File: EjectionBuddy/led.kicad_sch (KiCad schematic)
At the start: 10 parts

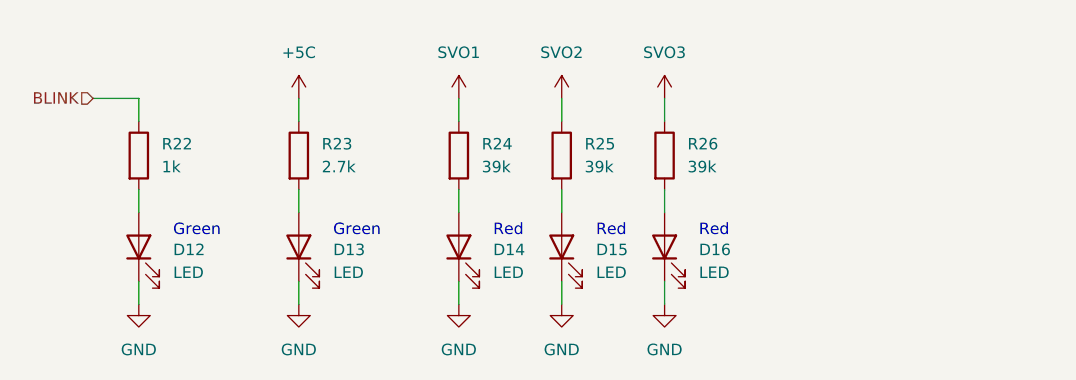
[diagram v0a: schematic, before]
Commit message: Side-mcu stm -> attiny, with improvements here and there
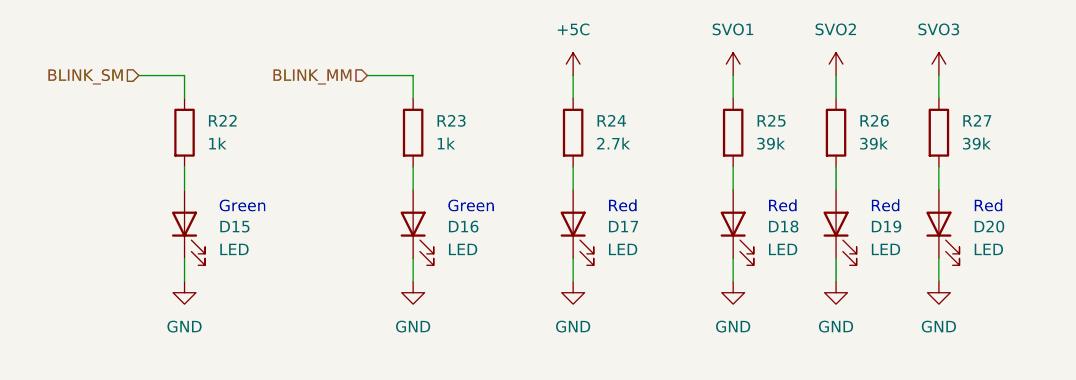
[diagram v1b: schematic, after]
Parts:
- added D15: LED, LED_SMD:LED_0603_1608Metric, symbol Device:LED
- added R22: 1k, Resistor_SMD:R_0603_1608Metric, symbol Device:R
- renumbered D12 to D16, D13 to D17, D14 to D18, D15 to D19, D16 to D20, R22 to R23, R23 to R24, R24 to R25, R25 to R26, R26 to R27
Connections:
- net GND: now also D15.1 (K)
- net BLINK renamed BLINK_MM
- new net: D15.2 (A), R22.2
- new net BLINK_SM: R22.1
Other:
- moved on the sheet: D16, D17, D18, D19, D20, R23, R24, R25, R26, R27

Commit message: Prodection version hw1.0 finished, with tidy-ups and bug-fixes
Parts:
- D15, D16: value LED -> LED_G
- D17, D18, D19, D20: value LED -> LED_R
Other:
- moved on the sheet: D19, D20, R26, R27
